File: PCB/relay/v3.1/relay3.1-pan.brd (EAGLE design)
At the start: 52.1 x 67.3 mm, 16 parts, among them K1 JS-M1-9V-5, K2 JS-M1-9V-5, Q1 BSP75, X1 22-23-20315.08S, X2 22-23-20315.08S

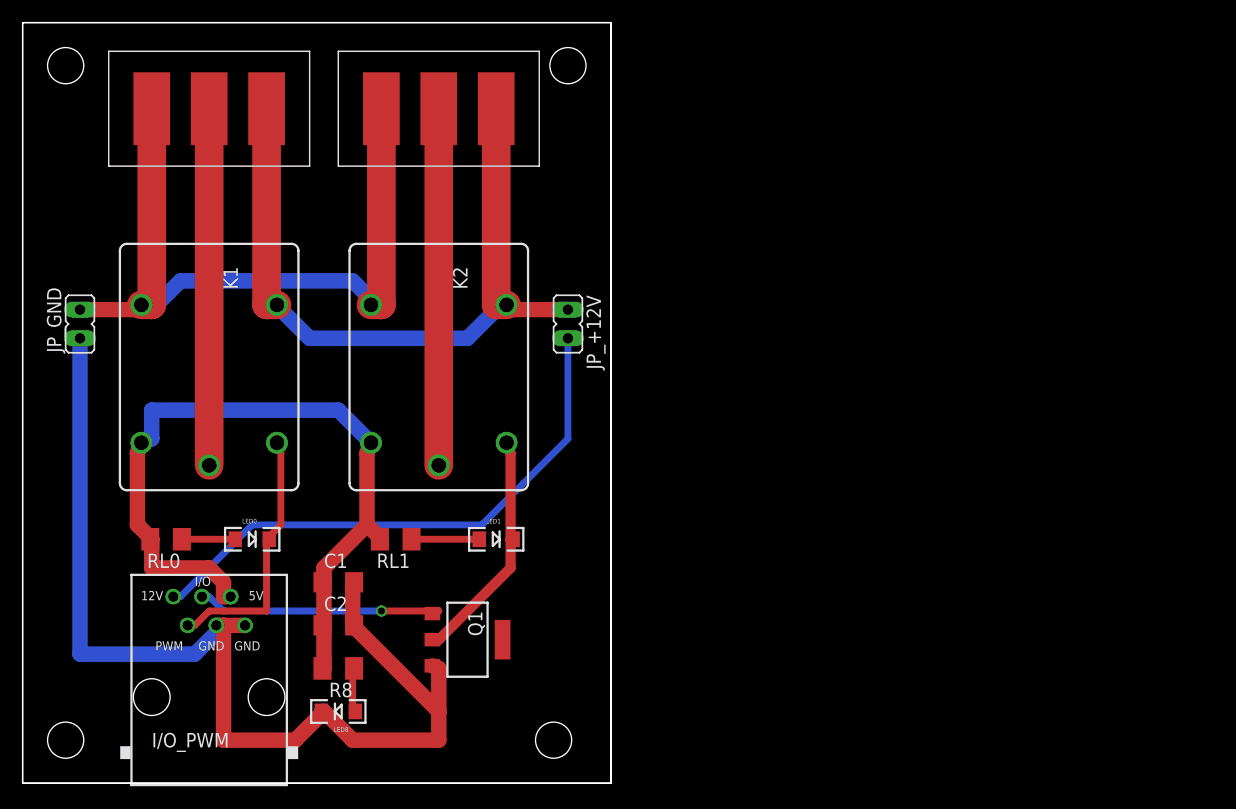
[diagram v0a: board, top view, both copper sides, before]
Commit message: Solar Decathlon V2 w/ current sense - panelized boards
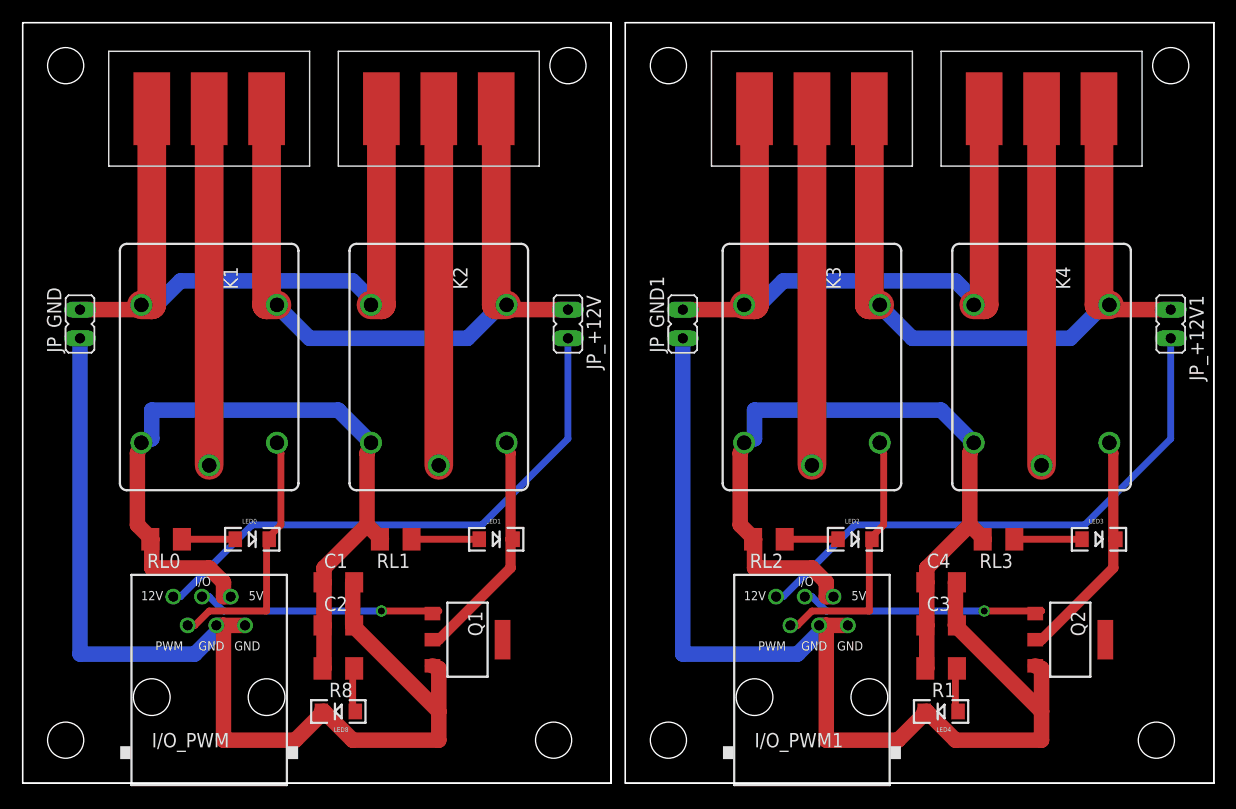
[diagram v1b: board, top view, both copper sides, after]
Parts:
- added C3: 100nF, rcl:C1206
- added C4: 10uF, rcl:C1206
- added I/O_PWM1: I2C 1, lpatiny:RJ12-STRAIGHT
- added JP_+12V1, JP_GND1: (no value), jumper:JP1
- added K3, K4: JS-M1-9V-5, relay:JS-M
- added LED2, LED3, LED4: (no value), SparkFun:LED-1206
- added Q2: BSP75, infineon:PG-SOT-223
- added R1, RL2, RL3: 1K, resistor:M1206
- added X3, X4: 22-23-20315.08S, lpatiny:3-PIN-5.08S
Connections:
- new net +12V1: I/O_PWM1.+12V, JP_+12V1.2
- new net +12VRELAY1: JP_+12V1.1, K3.NO, K4.NO, X3.1, X4.1
- new net +5V1: C3.1, C4.1, I/O_PWM1.+5V, K3.2, K4.2, R1.2, RL2.2, RL3.2
- new net GND1: C3.2, C4.2, I/O_PWM1.GND1, I/O_PWM1.GND2, JP_GND1.1, LED4.C, Q2.3
- new net GNDRELAY1: JP_GND1.2, K3.NC, K4.NC, X3.3, X4.3
- new net I/O1: I/O_PWM1.I/O, Q2.1
- new net N$3: K4.1, LED3.C, Q2.2
- new net N$6: LED2.A, RL2.1
- new net N$7: LED3.A, RL3.1
- new net N$8: LED4.A, R1.1
- new net N$9: K4.C, X3.2
- new net POWER2: K3.C, X4.2
- new net PWM1: I/O_PWM1.PWM, K3.1, LED2.C
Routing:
- net GND1: track 0.00 -> 98.2 mm
- net +5V1: track 0.00 -> 68.6 mm
- net +12VRELAY1: track 0.00 -> 64.9 mm
- net GNDRELAY1: track 0.00 -> 64.7 mm
- net +12V1: track 0.00 -> 49.6 mm
- net POWER2: track 0.00 -> 31.6 mm
- net N$9: track 0.00 -> 31.6 mm
- net PWM1: track 0.00 -> 23.2 mm
- net I/O1: track 0.00 -> 22.1 mm, vias 0 -> 1
- net N$3: track 0.00 -> 20.9 mm
- net N$7: track 0.00 -> 6.35 mm
- net N$6: track 0.00 -> 5.08 mm
- net N$8: track 0.00 -> 4.17 mm
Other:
- board size 52.1 x 67.3 mm -> 105.4 x 67.3 mm
- board text added: "C1"
- board text added: "C2"
- board text added: "I/O_PWM"
- board text added: "JP_+12V"
- board text added: "JP_GND"
- board text added: "K1"
- board text added: "K2"
- board text added: "LED0"
- board text added: "LED1"
- board text added: "LED8"
- board text added: "Q1"
- board text added: "R8"
- board text added: "RL0"
- board text added: "RL1"
